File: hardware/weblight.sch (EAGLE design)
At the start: 16 parts, among them U1 ATtiny85-20SU

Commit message: Add fiducials. Move bottom text. Handle DirtyPCB DRU. Ver 1.0
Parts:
- added FID1, FID2: FIDUCIAL, adafruit:FIDUCIAL
- D3, D4: value (none) -> 1SS367
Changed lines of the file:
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@@
 <grid distance="0.1" unitdist="inch" unit="inch" style="lines" multiple="1" display="no" altdistance="0.01" altunitdist="inch" altunit="inch"/>
 <layers>
-<layer number="1" name="Top" color="4" fill="1" visible="no" active="no"/>
-<layer number="16" name="Bottom" color="1" fill="1" visible="no" active="no"/>
-<layer number="17" name="Pads" color="2" fill="1" visible="no" active="no"/>
-<layer number="18" name="Vias" color="2" fill="1" visible="no" active="no"/>
-<layer number="19" name="Unrouted" color="6" fill="1" visible="no" active="no"/>
-<layer number="20" name="Dimension" color="15" fill="1" visible="no" active="no"/>
-<layer number="21" name="tPlace" color="7" fill="1" visible="no" active="no"/>
-<layer number="22" name="bPlace" color="7" fill="1" visible="no" active="no"/>
-<layer number="23" name="tOrigins" color="15" fill="1" visible="no" active="no"/>
-<layer number="24" name="bOrigins" color="15" fill="1" visible="no" active="no"/>
-<layer number="25" name="tNames" color="7" fill="1" visible="no" active="no"/>
-<layer number="26" name="bNames" color="7" fill="1" visible="no" active="no"/>
-<layer number="27" name="tValues" color="7" fill="1" visible="no" active="no"/>
-<layer number="28" name="bValues" color="7" fill="1" visible="no" active="no"/>
+<layer number="1" name="Top" color="4" fill="1" visible="yes" active="no"/>
+<layer number="16" name="Bottom" color="1" fill="1" visible="yes" active="no"/>
+<layer number="17" name="Pads" color="2" fill="1" visible="yes" active="no"/>
+<layer number="18" name="Vias" color="2" fill="1" visible="yes" active="no"/>
+<layer number="19" name="Unrouted" color="6" fill="1" visible="yes" active="no"/>
+<layer number="20" name="Dimension" color="15" fill="1" visible="yes" active="no"/>
+<layer number="21" name="tPlace" color="7" fill="1" visible="yes" active="no"/>
+<layer number="22" name="bPlace" color="7" fill="1" visible="yes" active="no"/>
+<layer number="23" name="tOrigins" color="15" fill="1" visible="yes" active="no"/>
+<layer number="24" name="bOrigins" color="15" fill="1" visible="yes" active="no"/>
+<layer number="25" name="tNames" color="7" fill="1" visible="yes" active="no"/>
+<layer number="26" name="bNames" color="7" fill="1" visible="yes" active="no"/>
+<layer number="27" name="tValues" color="7" fill="1" visible="yes" active="no"/>
+<layer number="28" name="bValues" color="7" fill="1" visible="yes" active="no"/>
 <layer number="29" name="tStop" color="7" fill="3" visible="no" active="no"/>
 <layer number="30" name="bStop" color="7" fill="6" visible="no" active="no"/>
@@
 <layer number="35" name="tGlue" color="7" fill="4" visible="no" active="no"/>
 <layer number="36" name="bGlue" color="7" fill="5" visible="no" active="no"/>
-<layer number="37" name="tTest" color="7" fill="1" visible="no" active="no"/>
-<layer number="38" name="bTest" color="7" fill="1" visible="no" active="no"/>
+<layer number="37" name="tTest" color="7" fill="1" visible="yes" active="no"/>
+<layer number="38" name="bTest" color="7" fill="1" visible="yes" active="no"/>
 <layer number="39" name="tKeepout" color="4" fill="11" visible="no" active="no"/>
 <layer number="40" name="bKeepout" color="1" fill="11" visible="no" active="no"/>
@@
 <layer number="44" name="Drills" color="7" fill="1" visible="no" active="no"/>
 <layer number="45" name="Holes" color="7" fill="1" visible="no" active="no"/>
-<layer number="46" name="Milling" color="3" fill="1" visible="no" active="no"/>
-<layer number="47" name="Measures" color="7" fill="1" visible="no" active="no"/>
-<layer number="48" name="Document" color="7" fill="1" visible="no" active="no"/>
-<layer number="49" name="Reference" color="7" fill="1" visible="no" active="no"/>
-<layer number="50" name="dxf" color="7" fill="1" visible="no" active="no"/>
-<layer number="51" name="tDocu" color="7" fill="1" visible="no" active="no"/>
-<layer number="52" name="bDocu" color="7" fill="1" visible="no" active="no"/>
-<layer number="53" name="tGND_GNDA" color="7" fill="9" visible="no" active="no"/>
-<layer number="54" name="bGND_GNDA" color="1" fill="9" visible="no" active="no"/>
-<layer number="56" name="wert" color="7" fill="1" visible="no" active="no"/>
-<layer number="57" name="tCAD" color="7" fill="1" visible="no" active="no"/>
-<layer number="59" name="tCarbon" color="7" fill="1" visible="no" active="no"/>
-<layer number="60" name="bCarbon" color="7" fill="1" visible="no" active="no"/>
+<layer number="46" name="Milling" color="3" fill="1" visible="yes" active="no"/>
+<layer number="47" name="Measures" color="7" fill="1" visible="yes" active="no"/>
+<layer number="48" name="Document" color="7" fill="1" visible="yes" active="no"/>
+<layer number="49" name="Reference" color="7" fill="1" visible="yes" active="no"/>
+<layer number="50" name="dxf" color="7" fill="1" visible="yes" active="no"/>
+<layer number="51" name="tDocu" color="7" fill="1" visible="yes" active="no"/>
+<layer number="52" name="bDocu" color="7" fill="1" visible="yes" active="no"/>
+<layer number="53" name="tGND_GNDA" color="7" fill="9" visible="yes" active="no"/>
+<layer number="54" name="bGND_GNDA" color="1" fill="9" visible="yes" active="no"/>
+<layer number="56" name="wert" color="7" fill="1" visible="yes" active="no"/>
+<layer number="57" name="tCAD" color="7" fill="1" visible="yes" active="no"/>
+<layer number="59" name="tCarbon" color="7" fill="1" visible="yes" active="no"/>
+<layer number="60" name="bCarbon" color="7" fill="1" visible="yes" active="no"/>
 <layer number="90" name="Modules" color="5" fill="1" visible="yes" active="yes"/>
 <layer number="91" name="Nets" color="2" fill="1" visible="yes" active="yes"/>
@@
 <part name="J-TOP" library="SparkFun-Connectors" deviceset="USB" device="PCB_NOPASTE"/>
 <part name="J-BOT" library="SparkFun-Connectors" deviceset="USB" device="PCB_NOPASTE"/>
-<part name="D3" library="microbuilder" deviceset="DIODE" device="SOD-323"/>
-<part name="D4" library="microbuilder" deviceset="DIODE" device="SOD-323"/>
+<part name="D3" library="microbuilder" deviceset="DIODE" device="SOD-323" value="1SS367"/>
+<part name="D4" library="microbuilder" deviceset="DIODE" device="SOD-323" value="1SS367"/>
+<part name="FID1" library="adafruit" deviceset="FIDUCIAL" device=""/>
+<part name="FID2" library="adafruit" deviceset="FIDUCIAL" device=""/>
 </parts>
 <sheets>
@@
 <instance part="D3" gate="G$1" x="-71.12" y="58.42"/>
 <instance part="D4" gate="G$1" x="-71.12" y="40.64"/>
+<instance part="FID1" gate="G$1" x="43.18" y="35.56"/>
+<instance part="FID2" gate="G$1" x="50.8" y="35.56"/>
 </instances>
 <busses>

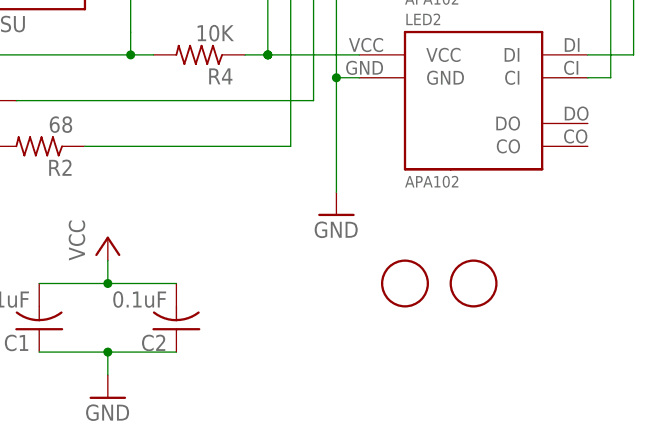
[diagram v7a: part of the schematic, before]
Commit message: Fix #39: one fiducial under U1; 1.0.1
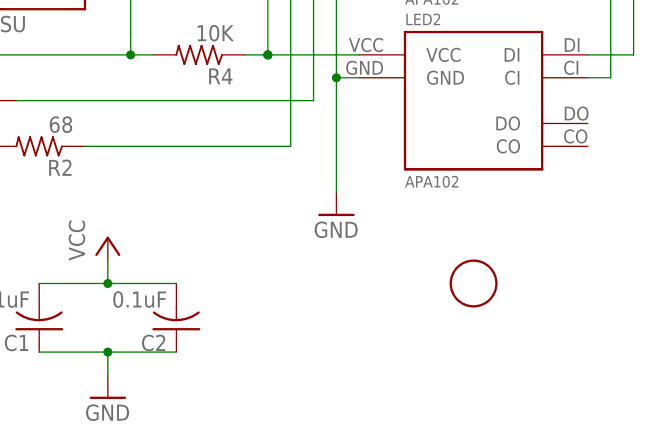
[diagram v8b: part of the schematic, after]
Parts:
- removed FID2: FIDUCIAL, adafruit:FIDUCIAL
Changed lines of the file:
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@@
 <?xml version="1.0" encoding="utf-8"?>
 <!DOCTYPE eagle SYSTEM "eagle.dtd">
-<eagle version="7.5.0">
+<eagle version="7.6.0">
 <drawing>
 <settings>
@@
 <grid distance="0.1" unitdist="inch" unit="inch" style="lines" multiple="1" display="no" altdistance="0.01" altunitdist="inch" altunit="inch"/>
 <layers>
-<layer number="1" name="Top" color="4" fill="1" visible="yes" active="no"/>
-<layer number="16" name="Bottom" color="1" fill="1" visible="yes" active="no"/>
-<layer number="17" name="Pads" color="2" fill="1" visible="yes" active="no"/>
-<layer number="18" name="Vias" color="2" fill="1" visible="yes" active="no"/>
-<layer number="19" name="Unrouted" color="6" fill="1" visible="yes" active="no"/>
-<layer number="20" name="Dimension" color="15" fill="1" visible="yes" active="no"/>
-<layer number="21" name="tPlace" color="7" fill="1" visible="yes" active="no"/>
-<layer number="22" name="bPlace" color="7" fill="1" visible="yes" active="no"/>
-<layer number="23" name="tOrigins" color="15" fill="1" visible="yes" active="no"/>
-<layer number="24" name="bOrigins" color="15" fill="1" visible="yes" active="no"/>
-<layer number="25" name="tNames" color="7" fill="1" visible="yes" active="no"/>
-<layer number="26" name="bNames" color="7" fill="1" visible="yes" active="no"/>
-<layer number="27" name="tValues" color="7" fill="1" visible="yes" active="no"/>
-<layer number="28" name="bValues" color="7" fill="1" visible="yes" active="no"/>
+<layer number="1" name="Top" color="4" fill="1" visible="no" active="no"/>
+<layer number="16" name="Bottom" color="1" fill="1" visible="no" active="no"/>
+<layer number="17" name="Pads" color="2" fill="1" visible="no" active="no"/>
+<layer number="18" name="Vias" color="2" fill="1" visible="no" active="no"/>
+<layer number="19" name="Unrouted" color="6" fill="1" visible="no" active="no"/>
+<layer number="20" name="Dimension" color="15" fill="1" visible="no" active="no"/>
+<layer number="21" name="tPlace" color="7" fill="1" visible="no" active="no"/>
+<layer number="22" name="bPlace" color="7" fill="1" visible="no" active="no"/>
+<layer number="23" name="tOrigins" color="15" fill="1" visible="no" active="no"/>
+<layer number="24" name="bOrigins" color="15" fill="1" visible="no" active="no"/>
+<layer number="25" name="tNames" color="7" fill="1" visible="no" active="no"/>
+<layer number="26" name="bNames" color="7" fill="1" visible="no" active="no"/>
+<layer number="27" name="tValues" color="7" fill="1" visible="no" active="no"/>
+<layer number="28" name="bValues" color="7" fill="1" visible="no" active="no"/>
 <layer number="29" name="tStop" color="7" fill="3" visible="no" active="no"/>
 <layer number="30" name="bStop" color="7" fill="6" visible="no" active="no"/>
@@
 <layer number="35" name="tGlue" color="7" fill="4" visible="no" active="no"/>
 <layer number="36" name="bGlue" color="7" fill="5" visible="no" active="no"/>
-<layer number="37" name="tTest" color="7" fill="1" visible="yes" active="no"/>
-<layer number="38" name="bTest" color="7" fill="1" visible="yes" active="no"/>
+<layer number="37" name="tTest" color="7" fill="1" visible="no" active="no"/>
+<layer number="38" name="bTest" color="7" fill="1" visible="no" active="no"/>
 <layer number="39" name="tKeepout" color="4" fill="11" visible="no" active="no"/>
 <layer number="40" name="bKeepout" color="1" fill="11" visible="no" active="no"/>
@@
 <layer number="44" name="Drills" color="7" fill="1" visible="no" active="no"/>
 <layer number="45" name="Holes" color="7" fill="1" visible="no" active="no"/>
-<layer number="46" name="Milling" color="3" fill="1" visible="yes" active="no"/>
-<layer number="47" name="Measures" color="7" fill="1" visible="yes" active="no"/>
-<layer number="48" name="Document" color="7" fill="1" visible="yes" active="no"/>
-<layer number="49" name="Reference" color="7" fill="1" visible="yes" active="no"/>
-<layer number="50" name="dxf" color="7" fill="1" visible="yes" active="no"/>
-<layer number="51" name="tDocu" color="7" fill="1" visible="yes" active="no"/>
-<layer number="52" name="bDocu" color="7" fill="1" visible="yes" active="no"/>
-<layer number="53" name="tGND_GNDA" color="7" fill="9" visible="yes" active="no"/>
-<layer number="54" name="bGND_GNDA" color="1" fill="9" visible="yes" active="no"/>
-<layer number="56" name="wert" color="7" fill="1" visible="yes" active="no"/>
-<layer number="57" name="tCAD" color="7" fill="1" visible="yes" active="no"/>
-<layer number="59" name="tCarbon" color="7" fill="1" visible="yes" active="no"/>
-<layer number="60" name="bCarbon" color="7" fill="1" visible="yes" active="no"/>
+<layer number="46" name="Milling" color="3" fill="1" visible="no" active="no"/>
+<layer number="47" name="Measures" color="7" fill="1" visible="no" active="no"/>
+<layer number="48" name="Document" color="7" fill="1" visible="no" active="no"/>
+<layer number="49" name="Reference" color="7" fill="1" visible="no" active="no"/>
+<layer number="50" name="dxf" color="7" fill="1" visible="no" active="no"/>
+<layer number="51" name="tDocu" color="7" fill="1" visible="no" active="no"/>
+<layer number="52" name="bDocu" color="7" fill="1" visible="no" active="no"/>
+<layer number="53" name="tGND_GNDA" color="7" fill="9" visible="no" active="no"/>
+<layer number="54" name="bGND_GNDA" color="1" fill="9" visible="no" active="no"/>
+<layer number="56" name="wert" color="7" fill="1" visible="no" active="no"/>
+<layer number="57" name="tCAD" color="7" fill="1" visible="no" active="no"/>
+<layer number="59" name="tCarbon" color="7" fill="1" visible="no" active="no"/>
+<layer number="60" name="bCarbon" color="7" fill="1" visible="no" active="no"/>
 <layer number="90" name="Modules" color="5" fill="1" visible="yes" active="yes"/>
 <layer number="91" name="Nets" color="2" fill="1" visible="yes" active="yes"/>
@@
 <part name="D4" library="microbuilder" deviceset="DIODE" device="SOD-323" value="1SS367"/>
 <part name="FID1" library="adafruit" deviceset="FIDUCIAL" device=""/>
-<part name="FID2" library="adafruit" deviceset="FIDUCIAL" device=""/>
 </parts>
 <sheets>
@@
 <instance part="D3" gate="G$1" x="-71.12" y="58.42"/>
 <instance part="D4" gate="G$1" x="-71.12" y="40.64"/>
-<instance part="FID1" gate="G$1" x="43.18" y="35.56"/>
-<instance part="FID2" gate="G$1" x="50.8" y="35.56"/>
+<instance part="FID1" gate="G$1" x="50.8" y="35.56"/>
 </instances>
 <busses>
